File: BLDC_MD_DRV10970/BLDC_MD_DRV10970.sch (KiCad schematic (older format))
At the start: 1 part

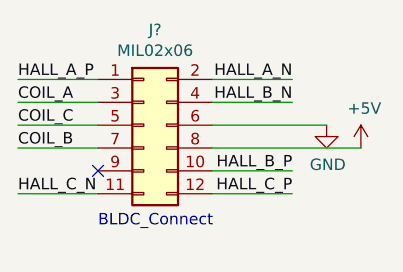
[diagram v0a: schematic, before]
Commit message: changed BLDC port from 12pin to 14pin connector, some pins will NOT be used.
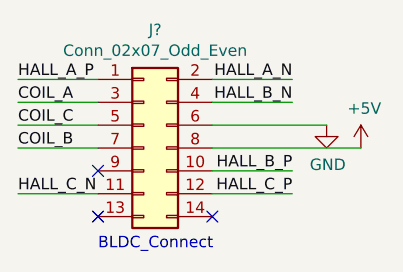
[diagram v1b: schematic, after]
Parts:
- removed J?: MIL02x06, symbol Connector_Generic:Conn_02x06_Odd_Even
- added J?: Conn_02x07_Odd_Even, symbol Connector_Generic:Conn_02x07_Odd_Even
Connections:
- net +5V: now also J?.8 (Pin_8)
- net COIL_A: now also J?.3 (Pin_3)
- net COIL_B: now also J?.7 (Pin_7)
- net COIL_C: now also J?.5 (Pin_5)
- net GND: now also J?.6 (Pin_6)
- net HALL_A_N: now also J?.2 (Pin_2)
- net HALL_A_P: now also J?.1 (Pin_1)
- net HALL_B_N: now also J?.4 (Pin_4)
- net HALL_B_P: now also J?.10 (Pin_10)
- net HALL_C_N: now also J?.11 (Pin_11)
- net HALL_C_P: now also J?.12 (Pin_12)
- no-connect marks 1 -> 3
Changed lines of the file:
@@
 Comment4 ""
 $EndDescr
-$Comp
-L Connector_Generic:Conn_02x06_Odd_Even J?
-U 1 1 5F0FEE49
-P 1300 1200
-F 0 "J?" H 1350 1617 50  0000 C CNN
-F 1 "MIL02x06" H 1350 1526 50  0000 C CNN
-F 2 "" H 1300 1200 50  0001 C CNN
-F 3 "~" H 1300 1200 50  0001 C CNN
-	1    1300 1200
-	1    0    0    -1
-$EndComp
 NoConn ~ 1100 1400
 Wire Wire Line
@@
 Text Label 1950 1500 2    50   ~ 0
 HALL_C_P
-Text Notes 1100 1650 0    50   ~ 0
+Text Notes 1100 1750 0    50   ~ 0
 BLDC_Connect
 $Comp
@@
 	1    0    0    -1
 $EndComp
+$Comp
+L Connector_Generic:Conn_02x07_Odd_Even J?
+U 1 1 5F105BC7
+P 1300 1300
+F 0 "J?" H 1350 1817 50  0000 C CNN
+F 1 "Conn_02x07_Odd_Even" H 1350 1726 50  0000 C CNN
+F 2 "" H 1300 1300 50  0001 C CNN
+F 3 "~" H 1300 1300 50  0001 C CNN
+	1    1300 1300
+	1    0    0    -1
+$EndComp
+NoConn ~ 1100 1600
+NoConn ~ 1600 1600
 $EndSCHEMATC

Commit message: changed BLDC_Connector type. from 02x06 to 02x07
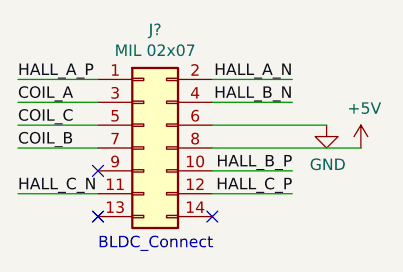
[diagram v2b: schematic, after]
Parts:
- J?: value Conn_02x07_Odd_Even -> MIL 02x07
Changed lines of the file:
@@
 P 1300 1300
 F 0 "J?" H 1350 1817 50  0000 C CNN
-F 1 "Conn_02x07_Odd_Even" H 1350 1726 50  0000 C CNN
+F 1 "MIL 02x07" H 1350 1726 50  0000 C CNN
 F 2 "" H 1300 1300 50  0001 C CNN
 F 3 "~" H 1300 1300 50  0001 C CNN

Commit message: done drowing schema.
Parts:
- added C1: 0.1uF, symbol Device:C
- added C2: 10uF, symbol Device:C
- added C3: 1000pF, symbol Device:C
- added C4: 1uF, symbol Device:C
- added C5: 2.2uF, symbol Device:C
- added IC1: DRV10970PWP, SOP65P640X120-25N, symbol LibraryLoader:DRV10970PWP
- added J2: Conn_01x08_Male, symbol Connector:Conn_01x08_Male
- added JP1, JP2, JP3: SolderJumper_3_Open, symbol Jumper:SolderJumper_3_Open
- added Q1, Q2, Q3, Q4: BSS138, SOT95P240X120-3N, symbol LibraryLoader:BSS138
- added R1, R11, R12, R14, R15, R2, R3, R4, R5, R6, R7, R8: 10k, symbol Device:R
- added R10, R9: 3.3k, symbol Device:R
- added R13: 20k, symbol Device:R
- gave numbers to parts that had none: 1
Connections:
- net +5V: now also J2.6 (Pin_6), JP1.3 (B), JP2.3 (B), JP3.3 (B), R10.1, R12.1, R5.1, R6.1, R7.1, R8.1, R9.1
- net COIL_A: now also IC1.14 (U)
- net COIL_B: now also IC1.13 (V)
- net COIL_C: now also IC1.11 (W)
- net GND: now also C2.1, C3.2, C5.1, IC1.12 (GND), IC1.25 (EP), J2.8 (Pin_8), JP1.1 (A), JP2.1 (A), JP3.1 (A), R13.2
- net HALL_A_N: now also IC1.3 (U_HN)
- net HALL_A_P: now also IC1.2 (U_HP)
- net HALL_B_N: now also IC1.5 (V_HN)
- net HALL_B_P: now also IC1.4 (V_HP)
- net HALL_C_N: now also IC1.7 (W_HN)
- net HALL_C_P: now also IC1.6 (W_HP)
- new net: C1.1, IC1.10 (CPN)
- new net: C5.2, IC1.16 (VINT)
- new net: C3.1, IC1.22 (RETRY)
- new net: C1.2, IC1.9 (CPP)
- new net: JP1.2 (C), R11.2
- new net: JP2.2 (C), R14.2
- new net: JP3.2 (C), R15.2
- new net +3V3: J2.5 (Pin_5), Q1.1, Q2.1, Q3.1, Q4.1, R1.1, R2.1, R3.1, R4.1
- new net BRKMOD: IC1.21 (BRKMOD), R15.1
- new net CMTMOD: IC1.20 (CMTMOD), R11.1
- new net CS: IC1.17 (CS), R13.1
- new net DAA: IC1.1 (DA), R14.1
- new net FG: IC1.24 (FG), Q1.3, R5.2, R9.2
- new net FG3V3: J2.1 (Pin_1), Q1.2, R1.2
- new net FR: IC1.23 (FR), Q2.3, R12.2, R6.2
- new net FR3V3: J2.2 (Pin_2), Q2.2, R2.2
- new net PWM: IC1.19 (PWM), Q3.3, R7.2
- new net PWM3V3: J2.3 (Pin_3), Q3.2, R3.2
- new net RD: IC1.18 (RD), Q4.3, R10.2, R8.2
- new net RD3V3: J2.4 (Pin_4), Q4.2, R4.2
- new net VCC: C2.2, C4.2, IC1.15 (VM), J2.7 (Pin_7)
- new net VCP: C4.1, IC1.8 (VCP)
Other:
- note added: "DRV10970"
- note added: "logic level converter"
- moved on the sheet: J1

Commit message: Related symbol and footprint
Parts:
- C1, C2, C3, C4, C5: footprint (none) -> Capacitor_SMD:C_0603_1608Metric
- IC1: footprint SOP65P640X120-25N -> LibraryLoader:SOP65P640X120-25N
- J1: footprint (none) -> Connector_PinHeader_2.54mm:PinHeader_2x07_P2.54mm_Horizontal
- J2: footprint (none) -> Connector_PinHeader_2.54mm:PinHeader_1x08_P2.54mm_Horizontal
- JP1, JP2, JP3: footprint (none) -> Jumper:SolderJumper-3_P2.0mm_Open_TrianglePad1.0x1.5mm
- Q1, Q2, Q3, Q4: footprint SOT95P240X120-3N -> LibraryLoader:SOT95P240X120-3N
- R1, R10, R11, R12, R13, R14, R15, R2, R3, R4, R5, R6, R7, R8, R9: footprint (none) -> Resistor_SMD:R_0603_1608Metric
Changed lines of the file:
@@
 F 0 "J1" H 1950 1917 50  0000 C CNN
 F 1 "MIL 02x07" H 1950 1826 50  0000 C CNN
-F 2 "" H 1900 1400 50  0001 C CNN
+F 2 "Connector_PinHeader_2.54mm:PinHeader_2x07_P2.54mm_Horizontal" H 1900 1400 50  0001 C CNN
 F 3 "~" H 1900 1400 50  0001 C CNN
 	1    1900 1400
@@
 F 0 "C1" H 3886 4104 50  0000 R CNN
 F 1 "0.1uF" H 3886 4195 50  0000 R CNN
-F 2 "" H 4038 4000 50  0001 C CNN
+F 2 "Capacitor_SMD:C_0603_1608Metric" H 4038 4000 50  0001 C CNN
 F 3 "~" H 4000 4150 50  0001 C CNN
 	1    4000 4150
@@
 F 0 "C2" H 6536 4404 50  0000 R CNN
 F 1 "10uF" H 6536 4495 50  0000 R CNN
-F 2 "" H 6688 4300 50  0001 C CNN
+F 2 "Capacitor_SMD:C_0603_1608Metric" H 6688 4300 50  0001 C CNN
 F 3 "~" H 6650 4450 50  0001 C CNN
 	1    6650 4450
@@
 F 0 "C4" H 6985 4404 50  0000 R CNN
 F 1 "1uF" H 6985 4495 50  0000 R CNN
-F 2 "" H 7138 4300 50  0001 C CNN
+F 2 "Capacitor_SMD:C_0603_1608Metric" H 7138 4300 50  0001 C CNN
 F 3 "~" H 7100 4450 50  0001 C CNN
 	1    7100 4450
@@
 F 0 "C5" H 7736 4304 50  0000 R CNN
 F 1 "2.2uF" H 7736 4395 50  0000 R CNN
-F 2 "" H 7888 4200 50  0001 C CNN
+F 2 "Capacitor_SMD:C_0603_1608Metric" H 7888 4200 50  0001 C CNN
 F 3 "~" H 7850 4350 50  0001 C CNN
 	1    7850 4350
@@
 F 0 "JP1" H 8950 3513 50  0000 C CNN
 F 1 "SolderJumper_3_Open" H 8950 3700 50  0000 C CNN
-F 2 "" H 8950 3400 50  0001 C CNN
+F 2 "Jumper:SolderJumper-3_P2.0mm_Open_TrianglePad1.0x1.5mm" H 8950 3400 50  0001 C CNN
 F 3 "~" H 8950 3400 50  0001 C CNN
 	1    8950 3400
@@
 F 0 "R11" H 9020 3146 50  0000 L CNN
 F 1 "10k" H 9020 3055 50  0000 L CNN
-F 2 "" V 8880 3100 50  0001 C CNN
+F 2 "Resistor_SMD:R_0603_1608Metric" V 8880 3100 50  0001 C CNN
 F 3 "~" H 8950 3100 50  0001 C CNN
 	1    8950 3100
@@
 F 0 "R14" H 10070 3146 50  0000 L CNN
 F 1 "10k" H 10070 3055 50  0000 L CNN
-F 2 "" V 9930 3100 50  0001 C CNN
+F 2 "Resistor_SMD:R_0603_1608Metric" V 9930 3100 50  0001 C CNN
 F 3 "~" H 10000 3100 50  0001 C CNN
 	1    10000 3100
@@
 F 0 "JP2" H 10000 3513 50  0000 C CNN
 F 1 "SolderJumper_3_Open" H 10000 3700 50  0000 C CNN
-F 2 "" H 10000 3400 50  0001 C CNN
+F 2 "Jumper:SolderJumper-3_P2.0mm_Open_TrianglePad1.0x1.5mm" H 10000 3400 50  0001 C CNN
 F 3 "~" H 10000 3400 50  0001 C CNN
 	1    10000 3400
@@
 F 0 "R12" H 9020 4246 50  0000 L CNN
 F 1 "10k" H 9020 4155 50  0000 L CNN
-F 2 "" V 8880 4200 50  0001 C CNN
+F 2 "Resistor_SMD:R_0603_1608Metric" V 8880 4200 50  0001 C CNN
 F 3 "~" H 8950 4200 50  0001 C CNN
 	1    8950 4200
@@
 F 0 "R9" H 6720 3296 50  0000 L CNN
 F 1 "3.3k" H 6720 3205 50  0000 L CNN
-F 2 "" V 6580 3250 50  0001 C CNN
+F 2 "Resistor_SMD:R_0603_1608Metric" V 6580 3250 50  0001 C CNN
 F 3 "~" H 6650 3250 50  0001 C CNN
 	1    6650 3250
@@
 F 0 "R10" H 6720 3896 50  0000 L CNN
 F 1 "3.3k" H 6720 3805 50  0000 L CNN
-F 2 "" V 6580 3850 50  0001 C CNN
+F 2 "Resistor_SMD:R_0603_1608Metric" V 6580 3850 50  0001 C CNN
 F 3 "~" H 6650 3850 50  0001 C CNN
 	1    6650 3850
@@
 F 0 "JP3" H 10050 4463 50  0000 C CNN
 F 1 "SolderJumper_3_Open" H 10050 4650 50  0000 C CNN
-F 2 "" H 10050 4350 50  0001 C CNN
+F 2 "Jumper:SolderJumper-3_P2.0mm_Open_TrianglePad1.0x1.5mm" H 10050 4350 50  0001 C CNN
 F 3 "~" H 10050 4350 50  0001 C CNN
 	1    10050 4350
@@
 F 0 "R15" H 10120 4096 50  0000 L CNN
 F 1 "10k" H 10120 4005 50  0000 L CNN
-F 2 "" V 9980 4050 50  0001 C CNN
+F 2 "Resistor_SMD:R_0603_1608Metric" V 9980 4050 50  0001 C CNN
 F 3 "~" H 10050 4050 50  0001 C CNN
 	1    10050 4050
@@
 F 0 "R13" H 9020 4896 50  0000 L CNN
 F 1 "20k" H 9020 4805 50  0000 L CNN
-F 2 "" V 8880 4850 50  0001 C CNN
+F 2 "Resistor_SMD:R_0603_1608Metric" V 8880 4850 50  0001 C CNN
 F 3 "~" H 8950 4850 50  0001 C CNN
 	1    8950 4850
@@
 F 0 "C3" H 7165 3796 50  0000 L CNN
 F 1 "1000pF" H 7165 3705 50  0000 L CNN
-F 2 "" H 7088 3600 50  0001 C CNN
+F 2 "Capacitor_SMD:C_0603_1608Metric" H 7088 3600 50  0001 C CNN
 F 3 "~" H 7050 3750 50  0001 C CNN
 	1    7050 3750
@@
 F 0 "J2" H 3858 1831 50  0000 C CNN
 F 1 "Conn_01x08_Male" H 3858 1740 50  0000 C CNN
-F 2 "" H 3750 1350 50  0001 C CNN
+F 2 "Connector_PinHeader_2.54mm:PinHeader_1x08_P2.54mm_Horizontal" H 3750 1350 50  0001 C CNN
 F 3 "~" H 3750 1350 50  0001 C CNN
 	1    3750 1350
@@
 F 0 "Q1" V 2575 2950 50  0000 C CNN
 F 1 "BSS138" V 2666 2950 50  0000 C CNN
-F 2 "SOT95P240X120-3N" H 2550 2800 50  0001 L CNN
+F 2 "LibraryLoader:SOT95P240X120-3N" H 2550 2800 50  0001 L CNN
 F 3 "https://www.onsemi.com/pub/Collateral/BSS138-D.PDF" H 2550 2700 50  0001 L CNN
 F 4 "N-channel MOSFET,BSS138 0.2A 50V" H 2550 2600 50  0001 L CNN "Description"
@@
 F 0 "R1" H 1770 3046 50  0000 L CNN
 F 1 "10k" H 1770 2955 50  0000 L CNN
-F 2 "" V 1630 3000 50  0001 C CNN
+F 2 "Resistor_SMD:R_0603_1608Metric" V 1630 3000 50  0001 C CNN
 F 3 "~" H 1700 3000 50  0001 C CNN
 	1    1700 3000
@@
 F 0 "R5" H 2770 3046 50  0000 L CNN
 F 1 "10k" H 2770 2955 50  0000 L CNN
-F 2 "" V 2630 3000 50  0001 C CNN
+F 2 "Resistor_SMD:R_0603_1608Metric" V 2630 3000 50  0001 C CNN
 F 3 "~" H 2700 3000 50  0001 C CNN
 	1    2700 3000
@@
 F 0 "Q2" V 2575 3600 50  0000 C CNN
 F 1 "BSS138" V 2666 3600 50  0000 C CNN
-F 2 "SOT95P240X120-3N" H 2550 3450 50  0001 L CNN
+F 2 "LibraryLoader:SOT95P240X120-3N" H 2550 3450 50  0001 L CNN
 F 3 "https://www.onsemi.com/pub/Collateral/BSS138-D.PDF" H 2550 3350 50  0001 L CNN
 F 4 "N-channel MOSFET,BSS138 0.2A 50V" H 2550 3250 50  0001 L CNN "Description"
@@
 F 0 "R2" H 1770 3696 50  0000 L CNN
 F 1 "10k" H 1770 3605 50  0000 L CNN
-F 2 "" V 1630 3650 50  0001 C CNN
+F 2 "Resistor_SMD:R_0603_1608Metric" V 1630 3650 50  0001 C CNN
 F 3 "~" H 1700 3650 50  0001 C CNN
 	1    1700 3650
@@
 F 0 "R6" H 2770 3696 50  0000 L CNN
 F 1 "10k" H 2770 3605 50  0000 L CNN
-F 2 "" V 2630 3650 50  0001 C CNN
+F 2 "Resistor_SMD:R_0603_1608Metric" V 2630 3650 50  0001 C CNN
 F 3 "~" H 2700 3650 50  0001 C CNN
 	1    2700 3650
@@
 F 0 "Q3" V 2575 4250 50  0000 C CNN
 F 1 "BSS138" V 2666 4250 50  0000 C CNN
-F 2 "SOT95P240X120-3N" H 2550 4100 50  0001 L CNN
+F 2 "LibraryLoader:SOT95P240X120-3N" H 2550 4100 50  0001 L CNN
 F 3 "https://www.onsemi.com/pub/Collateral/BSS138-D.PDF" H 2550 4000 50  0001 L CNN
 F 4 "N-channel MOSFET,BSS138 0.2A 50V" H 2550 3900 50  0001 L CNN "Description"
@@
 F 0 "R3" H 1770 4346 50  0000 L CNN
 F 1 "10k" H 1770 4255 50  0000 L CNN
-F 2 "" V 1630 4300 50  0001 C CNN
+F 2 "Resistor_SMD:R_0603_1608Metric" V 1630 4300 50  0001 C CNN
 F 3 "~" H 1700 4300 50  0001 C CNN
 	1    1700 4300
@@
 F 0 "R7" H 2770 4346 50  0000 L CNN
 F 1 "10k" H 2770 4255 50  0000 L CNN
-F 2 "" V 2630 4300 50  0001 C CNN
+F 2 "Resistor_SMD:R_0603_1608Metric" V 2630 4300 50  0001 C CNN
 F 3 "~" H 2700 4300 50  0001 C CNN
 	1    2700 4300
@@
 F 0 "Q4" V 2575 4900 50  0000 C CNN
 F 1 "BSS138" V 2666 4900 50  0000 C CNN
-F 2 "SOT95P240X120-3N" H 2550 4750 50  0001 L CNN
+F 2 "LibraryLoader:SOT95P240X120-3N" H 2550 4750 50  0001 L CNN
 F 3 "https://www.onsemi.com/pub/Collateral/BSS138-D.PDF" H 2550 4650 50  0001 L CNN
 F 4 "N-channel MOSFET,BSS138 0.2A 50V" H 2550 4550 50  0001 L CNN "Description"
@@
 F 0 "R4" H 1770 4996 50  0000 L CNN
 F 1 "10k" H 1770 4905 50  0000 L CNN
-F 2 "" V 1630 4950 50  0001 C CNN
+F 2 "Resistor_SMD:R_0603_1608Metric" V 1630 4950 50  0001 C CNN
 F 3 "~" H 1700 4950 50  0001 C CNN
 	1    1700 4950
@@
 F 0 "R8" H 2770 4996 50  0000 L CNN
 F 1 "10k" H 2770 4905 50  0000 L CNN
-F 2 "" V 2630 4950 50  0001 C CNN
+F 2 "Resistor_SMD:R_0603_1608Metric" V 2630 4950 50  0001 C CNN
 F 3 "~" H 2700 4950 50  0001 C CNN
 	1    2700 4950
@@
 F 0 "IC1" H 5350 3665 50  0000 C CNN
 F 1 "DRV10970PWP" H 5350 3574 50  0000 C CNN
-F 2 "SOP65P640X120-25N" H 5800 3500 50  0001 L CNN
+F 2 "LibraryLoader:SOP65P640X120-25N" H 5800 3500 50  0001 L CNN
 F 3 "http://www.ti.com/lit/ds/symlink/drv10970.pdf" H 5800 3400 50  0001 L CNN
 F 4 "Motor / Motion / Ignition Controllers & Drivers 20W, 12V 3-phase sensored BLDC motor driver with single/3halls supported 24-HTSSOP -40 to 125" H 5800 3300 50  0001 L CNN "Description"

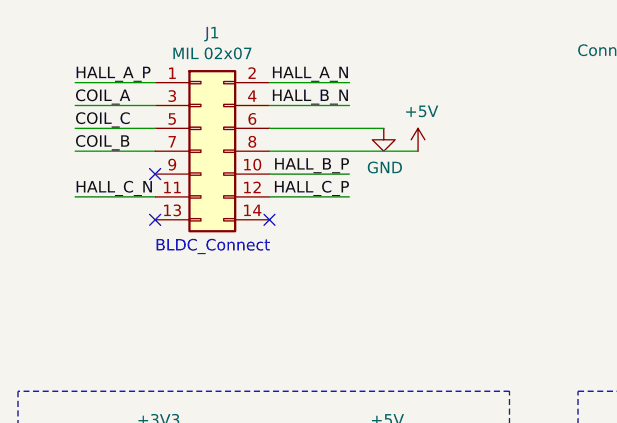
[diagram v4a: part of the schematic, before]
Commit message: routed all connections and exported board 3d files
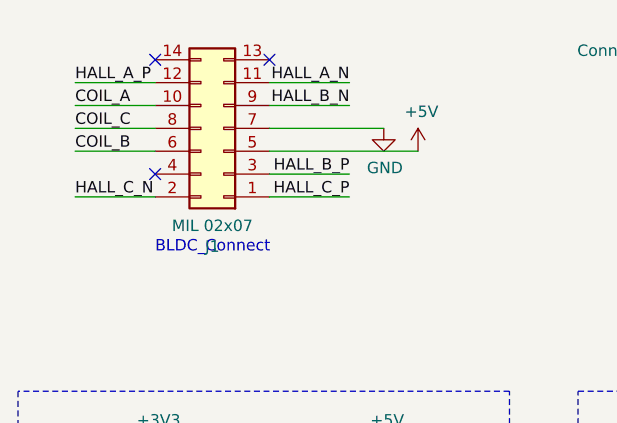
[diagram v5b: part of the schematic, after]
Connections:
- net +5V: now also J1.5 (Pin_5); no longer J1.8 (Pin_8)
- net COIL_A: now also J1.10 (Pin_10); no longer J1.3 (Pin_3)
- net COIL_B: now also J1.6 (Pin_6); no longer J1.7 (Pin_7)
- net COIL_C: now also J1.8 (Pin_8); no longer J1.5 (Pin_5)
- net GND: now also J1.7 (Pin_7); no longer J1.6 (Pin_6)
- net HALL_A_N: now also J1.11 (Pin_11); no longer J1.2 (Pin_2)
- net HALL_A_P: now also J1.12 (Pin_12); no longer J1.1 (Pin_1)
- net HALL_B_N: now also J1.9 (Pin_9); no longer J1.4 (Pin_4)
- net HALL_B_P: now also J1.3 (Pin_3); no longer J1.10 (Pin_10)
- net HALL_C_N: now also J1.2 (Pin_2); no longer J1.11 (Pin_11)
- net HALL_C_P: now also J1.1 (Pin_1); no longer J1.12 (Pin_12)
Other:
- moved on the sheet: J1
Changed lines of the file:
@@
 L Connector_Generic:Conn_02x07_Odd_Even J1
 U 1 1 5F105BC7
-P 1900 1400
-F 0 "J1" H 1950 1917 50  0000 C CNN
-F 1 "MIL 02x07" H 1950 1826 50  0000 C CNN
-F 2 "Connector_PinHeader_2.54mm:PinHeader_2x07_P2.54mm_Horizontal" H 1900 1400 50  0001 C CNN
-F 3 "~" H 1900 1400 50  0001 C CNN
-	1    1900 1400
-	1    0    0    -1
-$EndComp
-NoConn ~ 1700 1700
-NoConn ~ 2200 1700
+P 2000 1300
+F 0 "J1" H 2050 1817 50  0000 C CNN
+F 1 "MIL 02x07" H 2050 1726 50  0000 C CNN
+F 2 "Connector_PinHeader_2.54mm:PinHeader_2x07_P2.54mm_Horizontal" H 2000 1300 50  0001 C CNN
+F 3 "~" H 2000 1300 50  0001 C CNN
+	1    2000 1300
+	-1   0    0    1
+$EndComp
 $Comp
 L Device:C C1
@@
 	4100 4000 4000 4000
 $Comp
-L Device:C C2
-U 1 1 5F11273F
-P 6650 4450
-F 0 "C2" H 6536 4404 50  0000 R CNN
-F 1 "10uF" H 6536 4495 50  0000 R CNN
-F 2 "Capacitor_SMD:C_0603_1608Metric" H 6688 4300 50  0001 C CNN
-F 3 "~" H 6650 4450 50  0001 C CNN
-	1    6650 4450
-	1    0    0    1
-$EndComp
-Wire Wire Line
-	6650 4600 6650 4650
-$Comp
 L power:GND #PWR019
 U 1 1 5F113D34
@@
 	1    0    0    1
 $EndComp
-Wire Wire Line
-	6650 4300 7100 4300
-Connection ~ 6650 4300
 Wire Wire Line
 	7100 4600 7100 4750
@@
 	6300 4400 5950 4400
 Wire Wire Line
-	5950 4300 6650 4300
-Wire Wire Line
 	5950 4200 7850 4200
 Wire Wire Line
@@
 Text Notes 5400 5600 0    50   ~ 0
 DRV10970
+NoConn ~ 1700 1000
+NoConn ~ 2200 1000
+Wire Wire Line
+	6650 4600 6650 4650
+Wire Wire Line
+	5950 4300 6650 4300
+Wire Wire Line
+	6650 4300 7100 4300
+Connection ~ 6650 4300
+$Comp
+L Device:C C2
+U 1 1 5F11273F
+P 6650 4450
+F 0 "C2" H 6536 4404 50  0000 R CNN
+F 1 "10uF" H 6536 4495 50  0000 R CNN
+F 2 "Capacitor_SMD:C_0603_1608Metric" H 6688 4300 50  0001 C CNN
+F 3 "~" H 6650 4450 50  0001 C CNN
+	1    6650 4450
+	1    0    0    1
+$EndComp
 $EndSCHEMATC
